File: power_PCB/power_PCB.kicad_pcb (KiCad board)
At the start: 4 copper layers, 125 x 100 mm, 60 parts, among them J1 12V INPUT - 5 PAIRS, J2 LIGHT BOARD, J3 PUMP BOARD, J4 COOLER - 3 PAIRS, J5 BRAIN POWER, J6 COOLER CONTROL, Q1 CSD18540Q5B, U1 TPS54302DDCR, U2 TPS54302DDCR, U3 UCC27511ADBVR

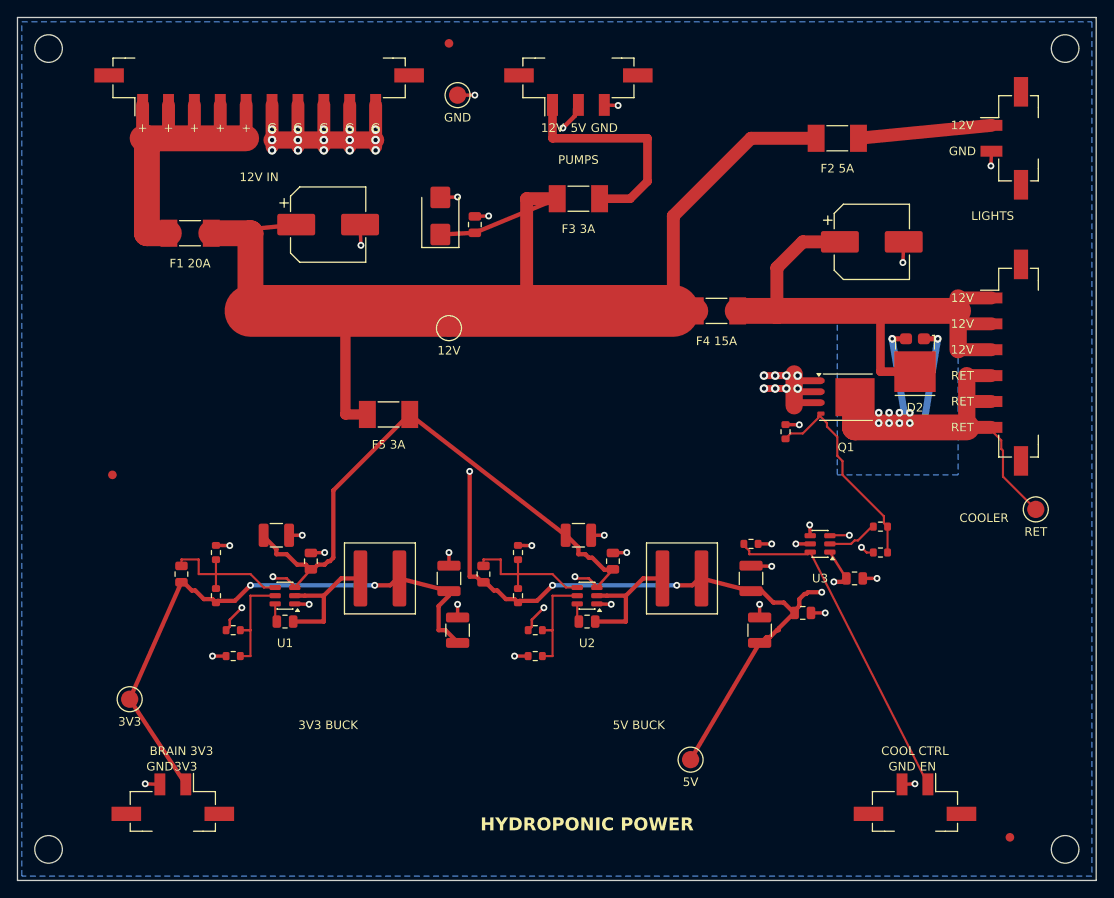
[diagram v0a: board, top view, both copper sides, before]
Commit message: Update four KiCad designs and include portable project libraries
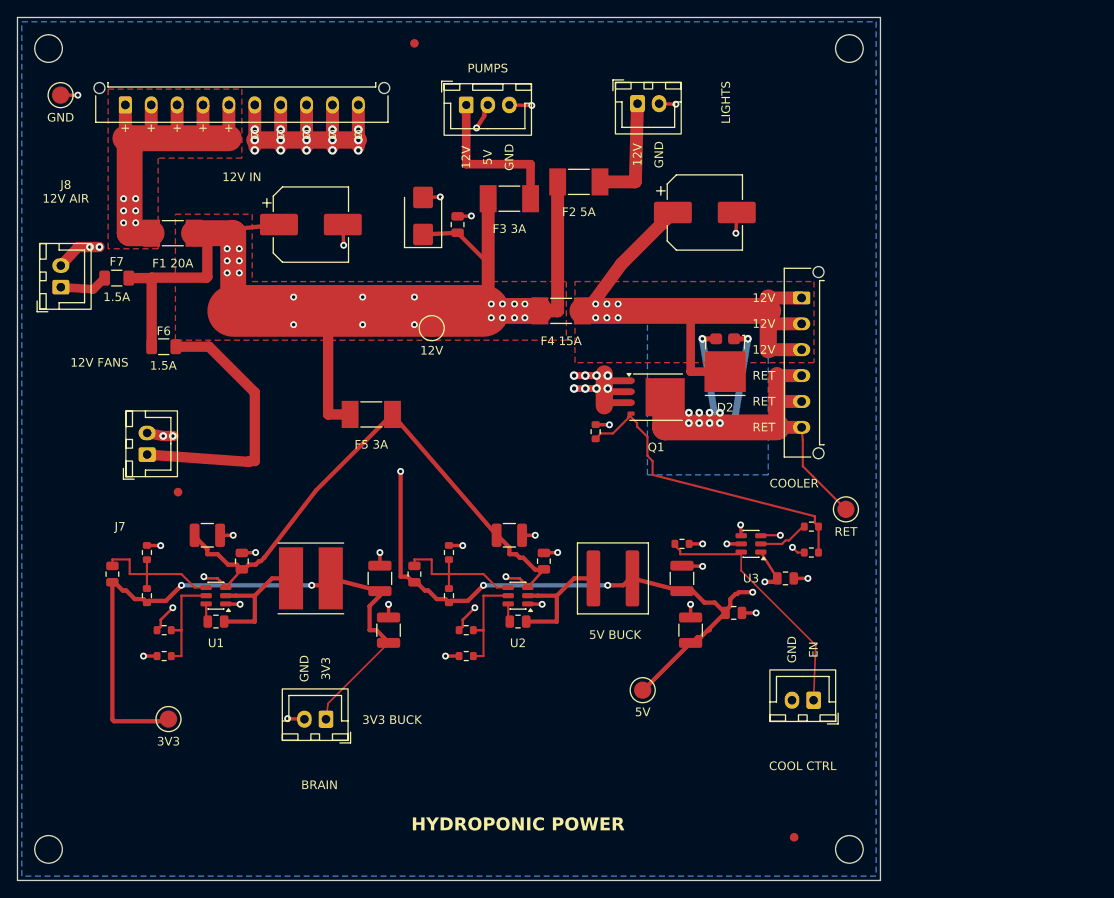
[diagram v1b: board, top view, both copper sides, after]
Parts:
- added F6: 1.5A FAST / FAN, Fuse:Fuse_1206_3216Metric, F.Cu at (52.0, 78.2)
- added F7: 1.5A FAST / AERATOR, Fuse:Fuse_1206_3216Metric, F.Cu at (46.5, 70.2)
- added J7: FANS TO BRAIN, Connector_JST:JST_XH_B2B-XH-A_1x02_P2.50mm_Vertical, F.Cu at (50.0, 90.7)
- added J8: AERATOR 12V, Connector_JST:JST_XH_B2B-XH-A_1x02_P2.50mm_Vertical, F.Cu at (40.0, 71.2)
- J1: footprint Connector_Molex:Molex_Micro-Fit_3.0_43650-1024_1x10-1MP_P3.00mm_Vertical -> Connector_Molex:Molex_Micro-Fit_3.0_43650-1015_1x10_P3.00mm_Vertical
- J2, J5, J6: footprint Connector_Molex:Molex_Micro-Fit_3.0_43650-0224_1x02-1MP_P3.00mm_Vertical -> Connector_JST:JST_XH_B2B-XH-A_1x02_P2.50mm_Vertical
- J3: footprint Connector_Molex:Molex_Micro-Fit_3.0_43650-0324_1x03-1MP_P3.00mm_Vertical -> Connector_JST:JST_XH_B3B-XH-A_1x03_P2.50mm_Vertical
- J4: footprint Connector_Molex:Molex_Micro-Fit_3.0_43650-0624_1x06-1MP_P3.00mm_Vertical -> Connector_Molex:Molex_Micro-Fit_3.0_43650-0615_1x06_P3.00mm_Vertical
- L1: footprint Inductor_SMD:L_Coilcraft_XAL7030-682 -> HydroPower:L_Bourns_SRP7030CA_7.6x7.8mm
- moved TP1 46.0 mm to (40.0, 49.0)
- moved J2 44.3 mm to (106.8, 50.0), turned to 0 degrees
- moved F2 30.4 mm to (100.0, 59.0)
- moved J4 26.2 mm to (125.9, 72.5)
- moved FID2 25.0 mm to (125.0, 135.0)
- moved H2 25.0 mm to (131.4, 43.6)
- moved H4 25.0 mm to (131.4, 136.4)
- moved D2 22.0 mm to (117.0, 80.0)
- moved Q1 22.0 mm to (109.0, 84.0)
- moved R12 22.0 mm to (102.0, 88.0)
- moved TP5 22.0 mm to (131.0, 97.0)
- moved J5 20.7 mm to (70.8, 121.3)
- moved C17 19.6 mm to (114.7, 62.6)
- moved F4 18.0 mm to (98.0, 74.0)
- moved J6 17.4 mm to (127.2, 119.1)
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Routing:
- net /P12V: track 200.7 -> 165.2 mm, vias 0 -> 20
- net /FAN_12V: track 0.00 -> 31.8 mm
- net Net-(Q1-G): track 24.8 -> 37.4 mm
- net /+5V: track 134.7 -> 123.9 mm
- net /COOL_EN: track 38.8 -> 29.4 mm
- net /GND: track 112.5 -> 121.0 mm, vias 52 -> 55
- net /PUMP_12V: track 26.2 -> 18.3 mm
- net /+3V3: track 68.1 -> 75.8 mm
- net /AER_12V: track 0.00 -> 5.62 mm
- net /COOL_12V: track 67.7 -> 65.4 mm, vias 0 -> 6
- net /LIGHT_12V: track 15.5 -> 13.1 mm
- net /LOGIC_12V: track 90.6 -> 88.2 mm
- net /VIN_12V: vias 0 -> 6
- added copper zone on F.Cu, net /COOL_12V
- added copper zone on In2.Cu, net /COOL_12V
- added copper zone on F.Cu, net /P12V
- added copper zone on In2.Cu, net /P12V
- added copper zone on F.Cu, net /VIN_12V
- added copper zone on In2.Cu, net /VIN_12V
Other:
- board size 125 x 100 mm -> 100 x 100 mm
- board text added: "1.5A"
- board text added: "12V AIR"
- board text added: "12V FANS"
- board text added: "BRAIN"
- board text removed: "BRAIN 3V3"
